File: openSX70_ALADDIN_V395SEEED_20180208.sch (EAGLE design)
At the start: 44 parts, among them J1 GND, Q1 2N7002, Q2 2N7002, U1 ATMEGA328P_TQFP, U3 BH1750FVI-TR, Y1 CSTCE8M00G52Z-R0

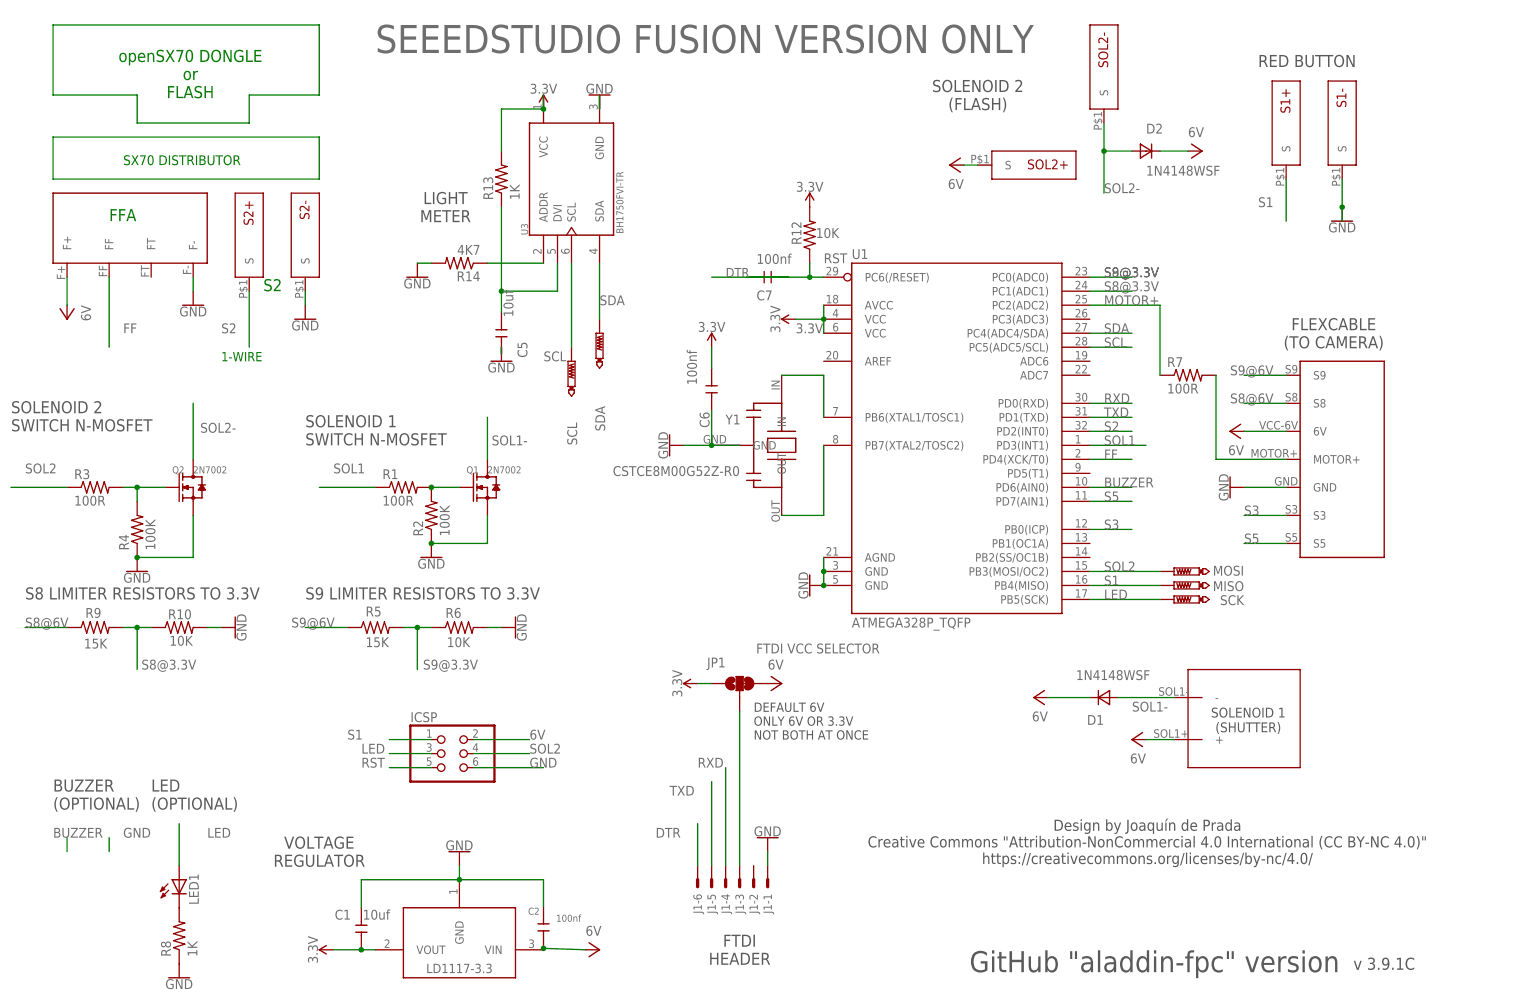
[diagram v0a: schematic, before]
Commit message: NEW VERSION 3.9.5S for SeeedStudio Fusion PCBA test
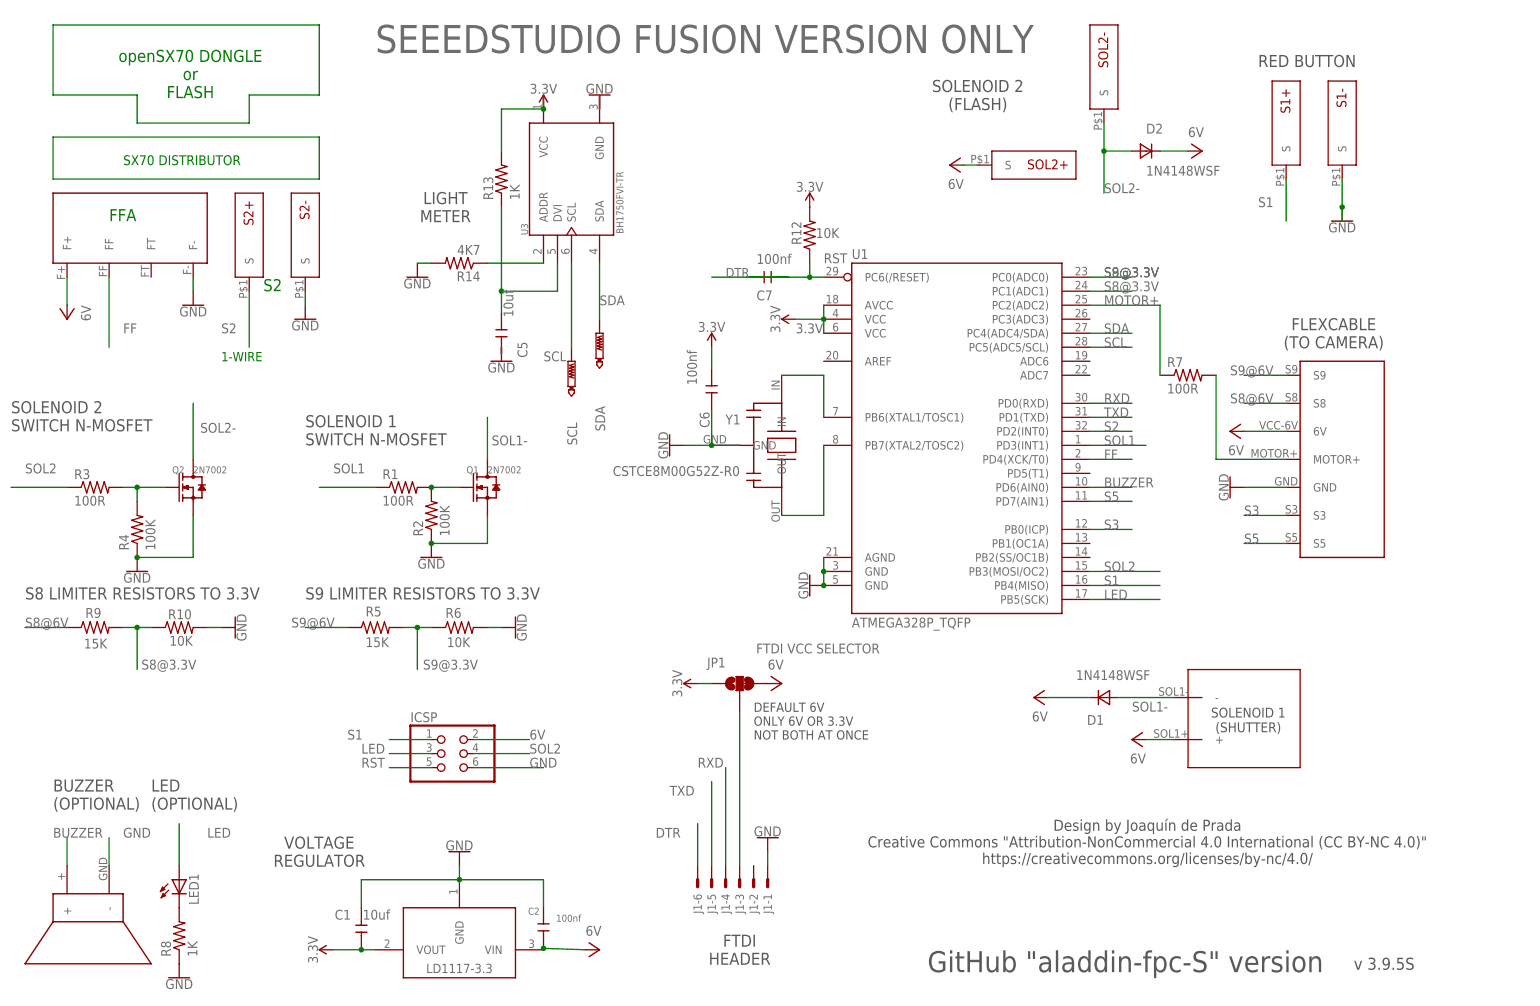
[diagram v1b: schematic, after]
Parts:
- removed MISO, MOSI, SCK: PTR1TP08R, testpad:PTR1TP08R
- added U$3: CSET8-5G_V2, openSX70:CSET8-5G_V2
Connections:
- net BUZZER: now also U$3.+
- net GND: now also U$3.-
- net LED: no longer SCK.TP
- net S1: no longer MISO.TP
- net SOL2: no longer MOSI.TP
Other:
- note added: "GitHub "aladdin-fpc-S" version"
- note added: "v 3.9.5S"
- note removed: "GitHub "aladdin-fpc" version"
- note removed: "v 3.9.1C"
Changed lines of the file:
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@@
 <part name="D1" library="zetex" library_urn="urn:adsk.eagle:library:418" deviceset="D" device="SOD323" package3d_urn="urn:adsk.eagle:package:30992/1" value="1N4148WSF"/>
 <part name="P+8" library="openSX70" deviceset="VCC" device="" value="6V"/>
-<part name="MOSI" library="testpad" library_urn="urn:adsk.eagle:library:385" deviceset="PTR1" device="TP08R" package3d_urn="urn:adsk.eagle:package:27956/1" value="PTR1TP08R"/>
-<part name="MISO" library="testpad" library_urn="urn:adsk.eagle:library:385" deviceset="PTR1" device="TP08R" package3d_urn="urn:adsk.eagle:package:27956/1" value="PTR1TP08R"/>
-<part name="SCK" library="testpad" library_urn="urn:adsk.eagle:library:385" deviceset="PTR1" device="TP08R" package3d_urn="urn:adsk.eagle:package:27956/1" value="PTR1TP08R"/>
 <part name="SDA" library="testpad" library_urn="urn:adsk.eagle:library:385" deviceset="PTR1" device="TP08R" package3d_urn="urn:adsk.eagle:package:27956/1" value="PTR1TP08R"/>
 <part name="SCL" library="testpad" library_urn="urn:adsk.eagle:library:385" deviceset="PTR1" device="TP08R" package3d_urn="urn:adsk.eagle:package:27956/1" value="PTR1TP08R"/>
 <part name="J1" library="con-omron" library_urn="urn:adsk.eagle:library:167" deviceset="XF2*-06?" device="25-1" package3d_urn="urn:adsk.eagle:package:9011/1" technology="L" value="GND"/>
 <part name="ICSP" library="pinhead" library_urn="urn:adsk.eagle:library:325" deviceset="PINHD-2X3" device="" package3d_urn="urn:adsk.eagle:package:22462/2"/>
+<part name="U$3" library="openSX70" deviceset="CSET8-5G_V2" device=""/>
 </parts>
 <sheets>
@@
 or
 FLASH</text>
-<text x="246.38" y="2.54" size="2.1844" layer="97" align="center">v 3.9.1C</text>
+<text x="246.38" y="2.54" size="2.1844" layer="97" align="center">v 3.9.5S</text>
 <text x="203.454" y="24.638" size="2.0066" layer="97" align="center">Design by Joaquín de Prada
 Creative Commons "Attribution-NonCommercial 4.0 International (CC BY-NC 4.0)"
 https://creativecommons.org/licenses/by-nc/4.0/</text>
-<text x="171.196" y="1.016" size="3.81" layer="97">GitHub "aladdin-fpc" version</text>
+<text x="163.576" y="1.016" size="3.81" layer="97">GitHub "aladdin-fpc-S" version</text>
 <text x="132.08" y="43.18" size="1.6764" layer="97">DEFAULT 6V
 ONLY 6V OR 3.3V
@@
 </instance>
 <instance part="P+8" gate="VCC" x="182.88" y="50.8" rot="R90"/>
-<instance part="MOSI" gate="G$1" x="208.28" y="73.66" smashed="yes" rot="R90">
-<attribute name="NAME" x="220.98" y="74.676" size="1.778" layer="95" rot="R180"/>
-<attribute name="TP_SIGNAL_NAME" x="210.82" y="74.93" size="1.778" layer="97" rot="R90"/>
-</instance>
-<instance part="MISO" gate="G$1" x="208.28" y="71.12" smashed="yes" rot="R90">
-<attribute name="NAME" x="220.98" y="71.882" size="1.778" layer="95" rot="R180"/>
-<attribute name="TP_SIGNAL_NAME" x="210.82" y="72.39" size="1.778" layer="97" rot="R90"/>
-</instance>
-<instance part="SCK" gate="G$1" x="208.28" y="68.58" smashed="yes" rot="R90">
-<attribute name="NAME" x="220.98" y="69.342" size="1.778" layer="95" rot="R180"/>
-<attribute name="TP_SIGNAL_NAME" x="210.82" y="69.85" size="1.778" layer="97" rot="R90"/>
-</instance>
 <instance part="SDA" gate="G$1" x="104.14" y="116.84" smashed="yes">
 <attribute name="NAME" x="105.156" y="99.06" size="1.778" layer="95" rot="R90"/>
@@
 </instance>
 <instance part="ICSP" gate="A" x="76.2" y="40.64"/>
+<instance part="U$3" gate="G$1" x="10.16" y="7.62" rot="R90"/>
 </instances>
 <busses>
@@
 <wire x1="193.04" y1="71.12" x2="205.74" y2="71.12" width="0.1524" layer="91"/>
 <label x="195.58" y="71.12" size="1.778" layer="95"/>
-<pinref part="MISO" gate="G$1" pin="TP"/>
 </segment>
 <segment>
@@
 <wire x1="193.04" y1="68.58" x2="205.74" y2="68.58" width="0.1524" layer="91"/>
 <label x="195.58" y="68.58" size="1.778" layer="95"/>
-<pinref part="SCK" gate="G$1" pin="TP"/>
 </segment>
 <segment>
@@
 <wire x1="193.04" y1="73.66" x2="205.74" y2="73.66" width="0.1524" layer="91"/>
 <label x="195.58" y="73.66" size="1.778" layer="95"/>
-<pinref part="MOSI" gate="G$1" pin="TP"/>
 </segment>
 <segment>
@@
 </segment>
 <segment>
-<wire x1="7.62" y1="22.86" x2="7.62" y2="25.4" width="0.1524" layer="91"/>
 <label x="5.08" y="25.4" size="1.778" layer="95"/>
+<pinref part="U$3" gate="G$1" pin="+"/>
+<wire x1="7.62" y1="25.4" x2="7.62" y2="20.32" width="0.1524" layer="91"/>
 </segment>
 </net>
@@
 </segment>
 <segment>
-<wire x1="15.24" y1="22.86" x2="15.24" y2="25.4" width="0.1524" layer="91"/>
 <label x="17.78" y="25.4" size="1.778" layer="95"/>
-</segment>
-<segment>
+<pinref part="U$3" gate="G$1" pin="-"/>
+<wire x1="15.24" y1="25.4" x2="15.24" y2="20.32" width="0.1524" layer="91"/>
+</segment>
+<segment>
